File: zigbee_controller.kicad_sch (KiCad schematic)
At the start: 73 parts, among them J1 Terminal MKDS, J10 Terminal MKDS, J11 Terminal MKDS, J12 Terminal MKDS, J13 Terminal MKDS, J3 Conn_01x06, J4 Conn_01x07, J5 Conn_01x05, P1 USB_C_Receptacle_GCT_USB4105, Q2 IRLB3813, Q3 IRLB3813, Q4 IRLB3813, Q5 IRLB3813, SW2 EN, SW4 Boot, U1 TPS54560, U2 ESP32-C6-MINI-1, U4 TC4427, U5 TC4427, U6 RT9080, U9 CH224K

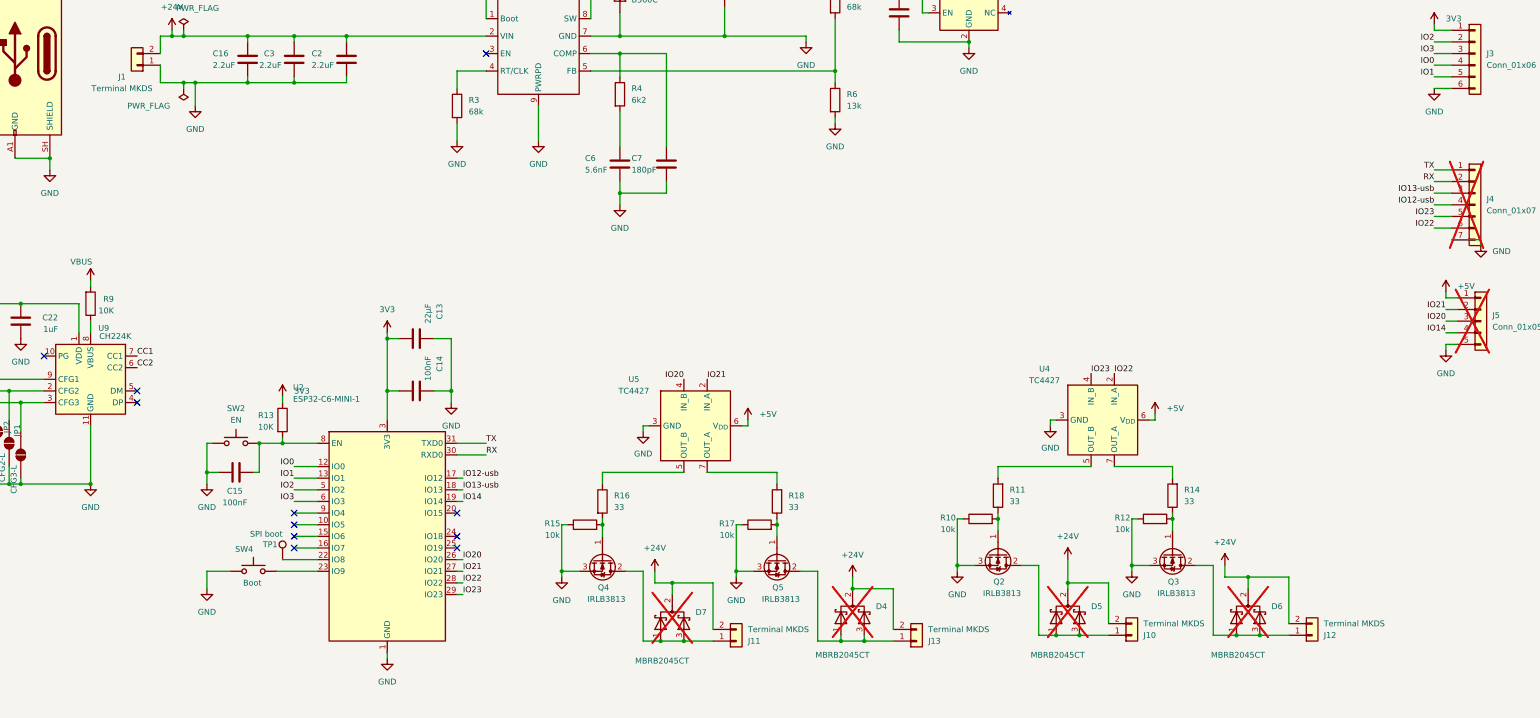
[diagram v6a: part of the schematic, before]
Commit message: Changed to KF635 and adapted the KF301, pre DRC check
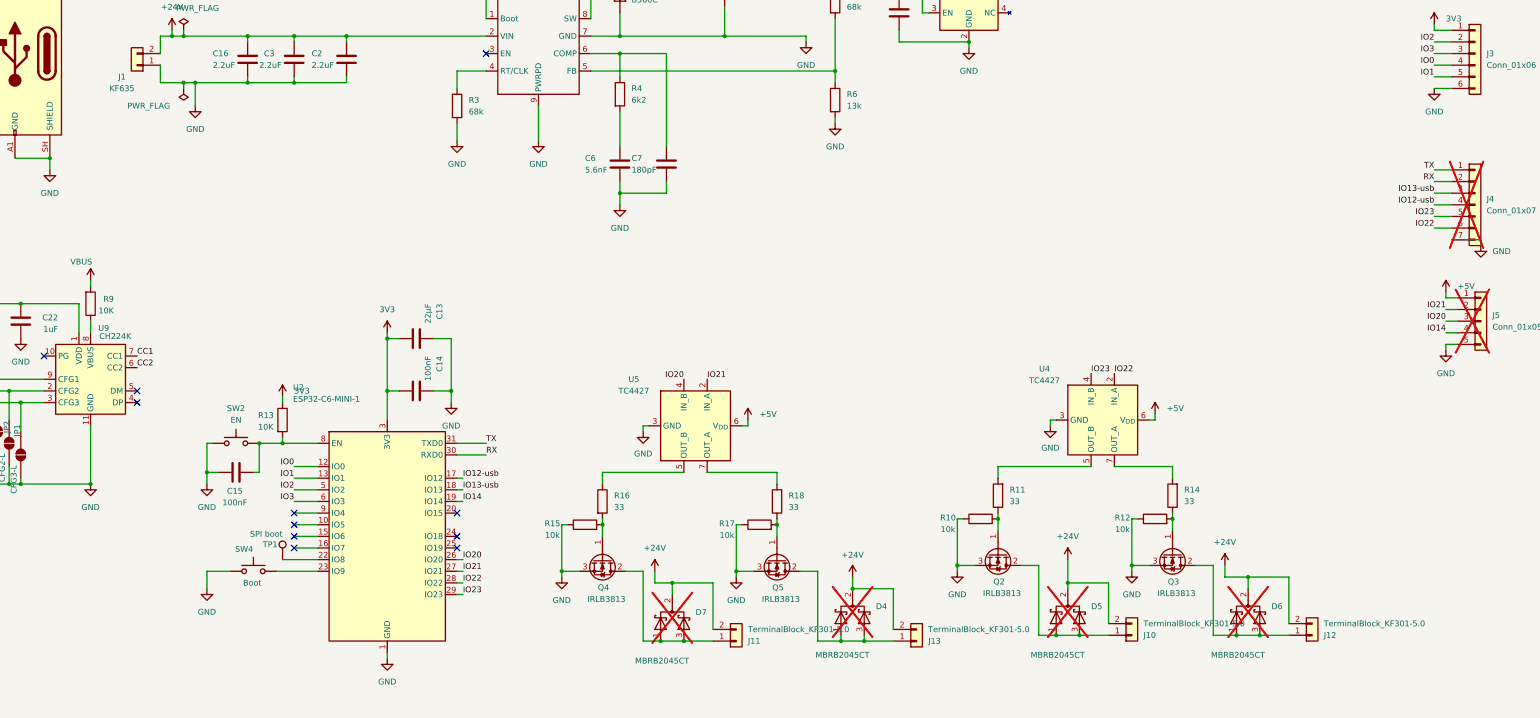
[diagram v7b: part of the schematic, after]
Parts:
- C22, C8: in_stock ordered -> yes
- C6, C7, D1: in_stock (none) -> ordered-20
- D2, D3, SW2, SW4: in_stock no -> ordered-20
- D4, D5, D6, D7: in_stock no -> yes-5
- D8, D9: in_stock (none) -> ordered-100
- J1: value Terminal MKDS -> KF635; footprint TerminalBlock:MKDS 1,5 2-5,08 P2 -> TerminalBlock:TerminalBlock_KF635-6.35; in_stock no -> ordered-2 (similar)
- J10, J11, J12, J13: value Terminal MKDS -> TerminalBlock_KF301-5.0; footprint TerminalBlock:MKDS 1,5 2-5,08 P2 -> TerminalBlock:TerminalBlock_KF301-5.0; in_stock no -> ordered-2 (similar)
- J3, R4: in_stock (none) -> yes
- JP1, JP10, JP2, JP3, JP4, JP5, JP6, JP7, JP8, JP9: in_stock (none) -> -
- L1, P1: in_stock no -> ordered-10
- Q2, Q3, Q4, Q5, U2, U4, U5: in_stock no -> ordered-2
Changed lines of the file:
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@@
 			)
 		)
+		(property "in_stock" "-"
+			(at 38.1 25.4 0)
+			(hide yes)
+			(show_name no)
+			(do_not_autoplace no)
+			(effects
+				(font
+					(size 1.27 1.27)
+				)
+			)
+		)
 		(pin "2"
 		)
@@
 			)
 		)
-		(property "in_stock" ""
+		(property "in_stock" "ordered-20"
 			(at 189.23 71.12 0)
 			(hide yes)
@@
 			)
 		)
+		(property "in_stock" "-"
+			(at 25.4 118.11 0)
+			(hide yes)
+			(show_name no)
+			(do_not_autoplace no)
+			(effects
+				(font
+					(size 1.27 1.27)
+				)
+			)
+		)
 		(pin "2"
 		)
@@
 			)
 		)
+		(property "in_stock" "-"
+			(at 55.88 132.08 0)
+			(hide yes)
+			(show_name no)
+			(do_not_autoplace no)
+			(effects
+				(font
+					(size 1.27 1.27)
+				)
+			)
+		)
 		(pin "2"
 		)
@@
 			)
 		)
-		(property "in_stock" "no"
+		(property "in_stock" "ordered-2"
 			(at 223.52 157.48 90)
 			(hide yes)
@@
 			)
 		)
+		(property "in_stock" "-"
+			(at 53.34 129.54 0)
+			(hide yes)
+			(show_name no)
+			(do_not_autoplace no)
+			(effects
+				(font
+					(size 1.27 1.27)
+				)
+			)
+		)
 		(pin "2"
 		)
@@
 			)
 		)
-		(property "in_stock" ""
+		(property "in_stock" "ordered-20"
 			(at 199.39 71.12 0)
 			(hide yes)
@@
 			)
 		)
-		(property "in_stock" "no"
+		(property "in_stock" "ordered-20"
 			(at 109.22 160.02 0)
 			(hide yes)
@@
 			)
 		)
-		(property "in_stock" "no"
+		(property "in_stock" "yes-5"
 			(at 240.03 168.91 90)
 			(hide yes)
@@
 			)
 		)
-		(property "in_stock" ""
+		(property "in_stock" "yes"
 			(at 375.92 46.99 0)
 			(hide yes)
@@
 			)
 		)
-		(property "in_stock" "no"
+		(property "in_stock" "ordered-2"
 			(at 309.88 156.21 90)
 			(hide yes)
@@
 			)
 		)
-		(property "in_stock" "no"
+		(property "in_stock" "ordered-2"
 			(at 138.43 152.4 0)
 			(hide yes)
@@
 			)
 		)
-		(property "in_stock" "no"
+		(property "in_stock" "ordered-10"
 			(at 57.15 46.99 0)
 			(hide yes)
@@
 			)
 		)
-		(property "in_stock" "no"
+		(property "in_stock" "yes-5"
 			(at 287.02 168.91 90)
 			(hide yes)
@@
 			)
 		)
-		(property "in_stock" "ordered"
+		(property "in_stock" "yes"
 			(at 250.19 38.1 0)
 			(hide yes)
@@
 			)
 		)
-		(property "Value" "Terminal MKDS"
+		(property "Value" "TerminalBlock_KF301-5.0"
 			(at 303.53 171.4501 0)
 			(show_name no)
@@
 			)
 		)
-		(property "Footprint" "TerminalBlock:MKDS 1,5 2-5,08 P2"
+		(property "Footprint" "TerminalBlock:TerminalBlock_KF301-5.0"
 			(at 300.99 173.99 0)
 			(hide yes)
@@
 			)
 		)
-		(property "in_stock" "no"
+		(property "in_stock" "ordered-2 (similar)"
 			(at 300.99 173.99 0)
 			(hide yes)
@@
 			)
 		)
-		(property "Value" "Terminal MKDS"
+		(property "Value" "KF635"
 			(at 80.518 54.61 0)
 			(show_name no)
@@
 			)
 		)
-		(property "Footprint" "TerminalBlock:MKDS 1,5 2-5,08 P2"
+		(property "Footprint" "TerminalBlock:TerminalBlock_KF635-6.35"
 			(at 83.82 49.53 0)
 			(hide yes)
@@
 			)
 		)
-		(property "in_stock" "no"
+		(property "in_stock" "ordered-2 (similar)"
 			(at 83.82 49.53 0)
 			(hide yes)
@@
 			)
 		)
-		(property "in_stock" ""
+		(property "in_stock" "yes"
 			(at 189.23 55.88 0)
 			(hide yes)
@@
 			)
 		)
+		(property "in_stock" "ordered-20"
+			(at 189.23 34.29 90)
+			(hide yes)
+			(show_name no)
+			(do_not_autoplace no)
+			(effects
+				(font
+					(size 1.27 1.27)
+				)
+			)
+		)
 		(pin "2"
 		)
@@
 			)
 		)
+		(property "in_stock" "-"
+			(at 20.32 31.75 0)
+			(hide yes)
+			(show_name no)
+			(do_not_autoplace no)
+			(effects
+				(font
+					(size 1.27 1.27)
+				)
+			)
+		)
 		(pin "2"
 		)
@@
 			)
 		)
-		(property "in_stock" "no"
+		(property "in_stock" "ordered-2"
 			(at 271.78 156.21 90)
 			(hide yes)
@@
 			)
 		)
-		(property "Value" "Terminal MKDS"
+		(property "Value" "TerminalBlock_KF301-5.0"
 			(at 217.17 172.7201 0)
 			(show_name no)
@@
 			)
 		)
-		(property "Footprint" "TerminalBlock:MKDS 1,5 2-5,08 P2"
+		(property "Footprint" "TerminalBlock:TerminalBlock_KF301-5.0"
 			(at 214.63 175.26 0)
 			(hide yes)
@@
 			)
 		)
-		(property "in_stock" "no"
+		(property "in_stock" "ordered-2 (similar)"
 			(at 214.63 175.26 0)
 			(hide yes)
@@
 			)
 		)
-		(property "in_stock" "ordered"
+		(property "in_stock" "yes"
 			(at 58.42 105.41 0)
 			(hide yes)
@@
 			)
 		)
-		(property "in_stock" "no"
+		(property "in_stock" "ordered-2"
 			(at 205.74 128.27 90)
 			(hide yes)
@@
 			)
 		)
-		(property "in_stock" "no"
+		(property "in_stock" "yes-5"
 			(at 200.66 170.18 90)
 			(hide yes)
@@
 			)
 		)
-		(property "in_stock" "no"
+		(property "in_stock" "yes-5"
 			(at 326.39 168.91 90)
 			(hide yes)
@@
 			)
 		)
-		(property "Value" "Terminal MKDS"
+		(property "Value" "TerminalBlock_KF301-5.0"
 			(at 342.9 171.4501 0)
 			(show_name no)
@@
 			)
 		)
-		(property "Footprint" "TerminalBlock:MKDS 1,5 2-5,08 P2"
+		(property "Footprint" "TerminalBlock:TerminalBlock_KF301-5.0"
 			(at 340.36 173.99 0)
 			(hide yes)
@@
 			)
 		)
-		(property "in_stock" "no"
+		(property "in_stock" "ordered-2 (similar)"
 			(at 340.36 173.99 0)
 			(hide yes)
@@
 			)
 		)
+		(property "in_stock" "-"
+			(at 44.45 123.19 0)
+			(hide yes)
+			(show_name no)
+			(do_not_autoplace no)
+			(effects
+				(font
+					(size 1.27 1.27)
+				)
+			)
+		)
 		(pin "2"
 		)
@@
 			)
 		)
-		(property "in_stock" "no"
+		(property "in_stock" "ordered-20"
 			(at 105.41 132.08 0)
 			(hide yes)
@@
 			)
 		)
+		(property "in_stock" "-"
+			(at 35.56 25.4 0)
+			(hide yes)
+			(show_name no)
+			(do_not_autoplace no)
+			(effects
+				(font
+					(size 1.27 1.27)
+				)
+			)
+		)
 		(pin "2"
 		)
@@
 			)
 		)
-		(property "in_stock" "no"
+		(property "in_stock" "ordered-10"
 			(at 195.58 24.13 90)
 			(hide yes)
@@
 			)
 		)
+		(property "in_stock" "-"
+			(at 58.42 134.62 0)
+			(hide yes)
+			(show_name no)
+			(do_not_autoplace no)
+			(effects
+				(font
+					(size 1.27 1.27)
+				)
+			)
+		)
 		(pin "2"
 		)
@@
 			)
 		)
-		(property "in_stock" "no"
+		(property "in_stock" "ordered-20"
 			(at 30.48 57.15 90)
 			(hide yes)
@@
 			)
 		)
-		(property "in_stock" "no"
+		(property "in_stock" "ordered-2"
 			(at 185.42 157.48 90)
 			(hide yes)
@@
 			)
 		)
+		(property "in_stock" "ordered-100"
+			(at 242.57 24.13 0)
+			(hide yes)
+			(show_name no)
+			(do_not_autoplace no)
+			(effects
+				(font
+					(size 1.27 1.27)
+				)
+			)
+		)
 		(pin "2"
 		)
@@
 			)
 		)
+		(property "in_stock" "-"
+			(at 34.29 120.65 0)
+			(hide yes)
+			(show_name no)
+			(do_not_autoplace no)
+			(effects
+				(font
+					(size 1.27 1.27)
+				)
+			)
+		)
 		(pin "2"
 		)
@@
 			)
 		)
-		(property "in_stock" "no"
+		(property "in_stock" "ordered-20"
 			(at 24.13 57.15 90)
 			(hide yes)
@@
 			)
 		)
-		(property "Value" "Terminal MKDS"
+		(property "Value" "TerminalBlock_KF301-5.0"
 			(at 256.54 172.7201 0)
 			(show_name no)
@@
 			)
 		)
-		(property "Footprint" "TerminalBlock:MKDS 1,5 2-5,08 P2"
+		(property "Footprint" "TerminalBlock:TerminalBlock_KF301-5.0"
 			(at 254 175.26 0)
 			(hide yes)
@@
 			)
 		)
-		(property "in_stock" "no"
+		(property "in_stock" "ordered-2 (similar)"
 			(at 254 175.26 0)
 			(hide yes)
@@
 			)
 		)
+		(property "in_stock" "-"
+			(at 40.64 25.4 0)
+			(hide yes)
+			(show_name no)
+			(do_not_autoplace no)
+			(effects
+				(font
+					(size 1.27 1.27)
+				)
+			)
+		)
 		(pin "2"
 		)
@@
 			)
 		)
+		(property "in_stock" "ordered-100"
+			(at 27.94 31.75 0)
+			(hide yes)
+			(show_name no)
+			(do_not_autoplace no)
+			(effects
+				(font
+					(size 1.27 1.27)
+				)
+			)
+		)
 		(pin "2"
 		)
@@
 			)
 		)
-		(property "in_stock" "no"
+		(property "in_stock" "ordered-2"
 			(at 294.64 127 90)
 			(hide yes)

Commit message: Final rev2
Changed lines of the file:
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@@
 		(in_pos_files yes)
 		(dnp no)
-		(fields_autoplaced yes)
 		(property "Reference" "#PWR045"
 			(at 248.92 26.67 0)
@@
 		)
 		(property "Value" "USB_5V"
-			(at 251.46 21.5899 0)
+			(at 249.682 19.558 0)
 			(show_name no)
 			(do_not_autoplace no)
@@
 		)
 		(property "Value" "PWR_FLAG"
-			(at 252.73 21.59 0)
+			(at 244.602 27.686 0)
 			(show_name no)
 			(do_not_autoplace no)
@@
 		(in_pos_files yes)
 		(dnp no)
-		(fields_autoplaced yes)
 		(property "Reference" "#PWR09"
 			(at 232.41 26.67 0)
@@
 		)
 		(property "Value" "+5V"
-			(at 234.95 21.5899 0)
+			(at 233.172 19.558 0)
 			(show_name no)
 			(do_not_autoplace no)
